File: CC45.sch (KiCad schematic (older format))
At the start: 20 parts, among them J1 AVR-ISP-6, SW1 SW_Push_Dual, U1 ATmega32U4-AU, U2 PRTR5V0U2X, X1 XTAL

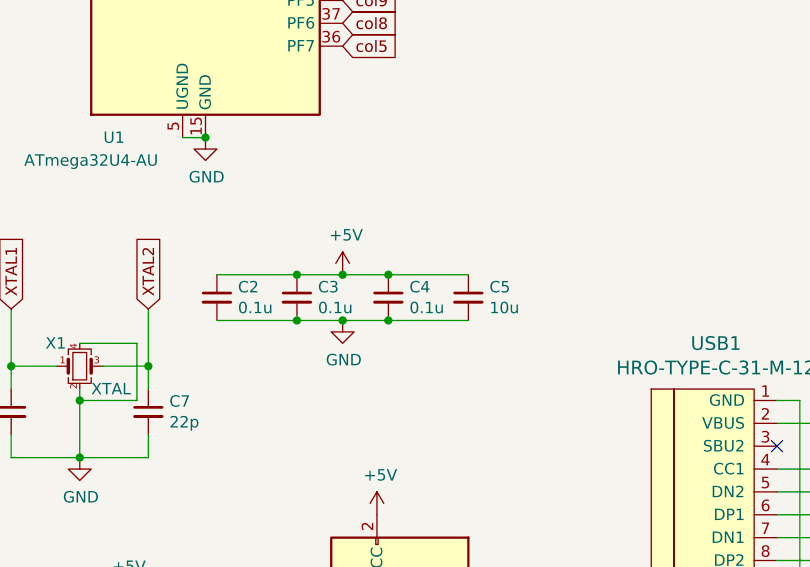
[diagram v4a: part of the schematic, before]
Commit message: Add a decoupling capacitor
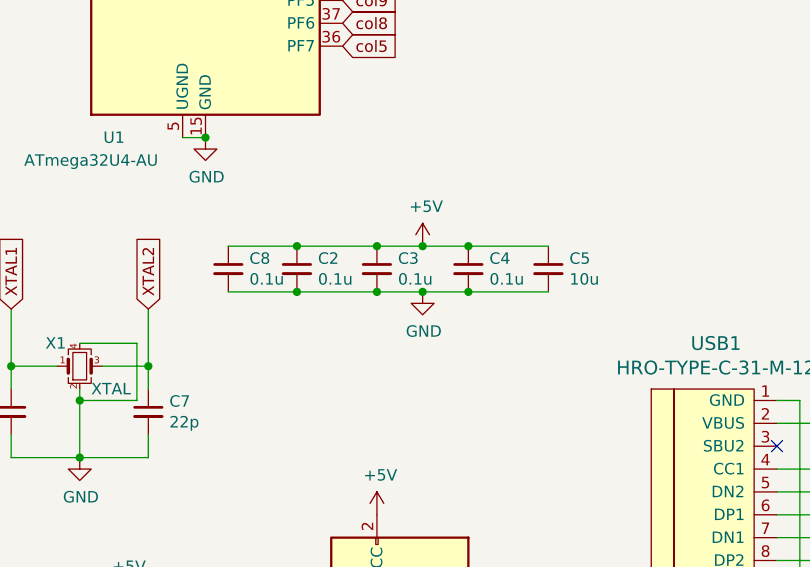
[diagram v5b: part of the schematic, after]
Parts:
- added C8: 0.1u, Capacitor_SMD:C_1206_3216Metric_Pad1.42x1.75mm_HandSolder, symbol Device:C_Small
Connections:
- net +5V: now also C8.1
- net GND: now also C8.2
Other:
- moved on the sheet: C2, C3, C4, C5

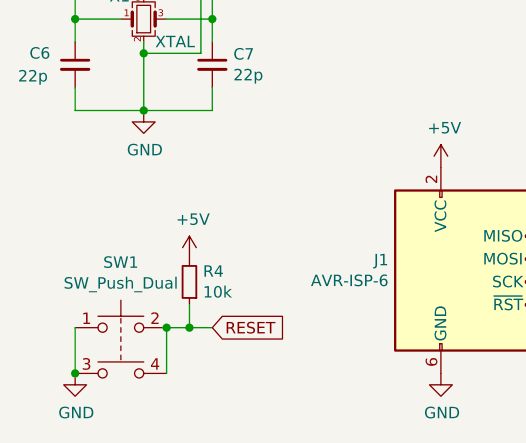
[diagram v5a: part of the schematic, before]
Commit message: Add fill zones
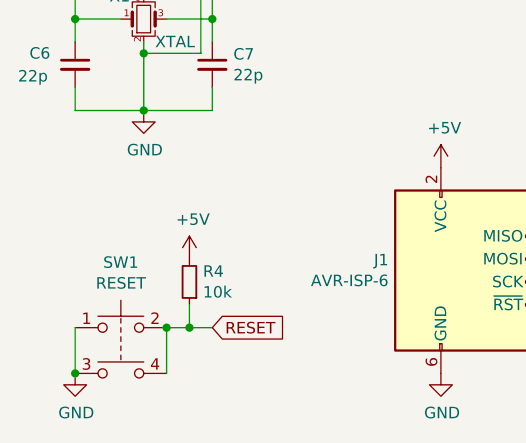
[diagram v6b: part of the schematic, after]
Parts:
- SW1: value SW_Push_Dual -> RESET
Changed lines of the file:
@@
 P 1300 7100
 F 0 "SW1" H 1300 7385 50  0000 C CNN
-F 1 "SW_Push_Dual" H 1300 7294 50  0000 C CNN
+F 1 "RESET" H 1300 7294 50  0000 C CNN
 F 2 "random-keyboard-parts:SKQG-1155865" H 1300 7300 50  0001 C CNN
 F 3 "~" H 1300 7300 50  0001 C CNN

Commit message: moving C4 closer to the mcu and adding JLC parts numbers
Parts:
- C1: LCSC (none) -> C1848
- C2, C3, C4, C8: LCSC (none) -> C24497
- C5: LCSC (none) -> C13585
- C6, C7: LCSC (none) -> C313096
- F1: LCSC (none) -> C151162
- R1, R4: LCSC (none) -> C17902
- R2, R3: LCSC (none) -> C17958
- R5, R6: LCSC (none) -> C26033
- SW1: LCSC (none) -> C318884
- U1: LCSC (none) -> C44854
- U2: LCSC (none) -> C78442
- X1: LCSC (none) -> C13738
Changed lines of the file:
@@
 F 2 "Capacitor_SMD:C_1206_3216Metric_Pad1.42x1.75mm_HandSolder" H 1100 5950 50  0001 C CNN
 F 3 "~" H 1100 5950 50  0001 C CNN
+F 4 "C313096" H 1100 5950 50  0001 C CNN "LCSC"
 	1    1100 5950
 	1    0    0    -1
@@
 F 2 "random-keyboard-parts:SKQG-1155865" H 1300 7300 50  0001 C CNN
 F 3 "~" H 1300 7300 50  0001 C CNN
+F 4 "C318884" H 1300 7100 50  0001 C CNN "LCSC"
 	1    1300 7100
 	1    0    0    -1
@@
 F 2 "Resistor_SMD:R_1206_3216Metric_Pad1.42x1.75mm_HandSolder" H 1600 6900 50  0001 C CNN
 F 3 "~" H 1600 6900 50  0001 C CNN
+F 4 "C17902" H 1600 6900 50  0001 C CNN "LCSC"
 	1    1600 6900
 	-1   0    0    1
@@
 F 2 "Fuse:Fuse_1206_3216Metric_Pad1.42x1.75mm_HandSolder" H 5200 5800 50  0001 L CNN
 F 3 "~" H 5150 6000 50  0001 C CNN
+F 4 "C151162" H 5150 6000 50  0001 C CNN "LCSC"
 	1    5150 6000
 	0    1    1    0
@@
 F 2 "Resistor_SMD:R_1206_3216Metric_Pad1.42x1.75mm_HandSolder" H 4800 6900 50  0001 C CNN
 F 3 "~" H 4800 6900 50  0001 C CNN
+F 4 "C26033" H 4800 6900 50  0001 C CNN "LCSC"
 	1    4800 6900
 	-1   0    0    1
@@
 F 2 "Resistor_SMD:R_1206_3216Metric_Pad1.42x1.75mm_HandSolder" H 5150 6900 50  0001 C CNN
 F 3 "~" H 5150 6900 50  0001 C CNN
+F 4 "C26033" H 5150 6900 50  0001 C CNN "LCSC"
 	1    5150 6900
 	-1   0    0    1
@@
 F 2 "Resistor_SMD:R_1206_3216Metric_Pad1.42x1.75mm_HandSolder" H 6400 6600 50  0001 C CNN
 F 3 "~" H 6400 6600 50  0001 C CNN
+F 4 "C17958" H 6400 6600 50  0001 C CNN "LCSC"
 	1    6400 6600
 	0    1    1    0
@@
 F 2 "Resistor_SMD:R_1206_3216Metric_Pad1.42x1.75mm_HandSolder" H 6400 6500 50  0001 C CNN
 F 3 "~" H 6400 6500 50  0001 C CNN
+F 4 "C17958" H 6400 6500 50  0001 C CNN "LCSC"
 	1    6400 6500
 	0    1    1    0
@@
 F 2 "random-keyboard-parts:SOT143B" H 5800 6900 60  0001 C CNN
 F 3 "" H 5800 6900 60  0001 C CNN
+F 4 "C78442" H 5800 6900 50  0001 C CNN "LCSC"
 	1    5800 6900
 	-1   0    0    1
@@
 F 2 "Capacitor_SMD:C_1206_3216Metric_Pad1.42x1.75mm_HandSolder" H 1700 5950 50  0001 C CNN
 F 3 "~" H 1700 5950 50  0001 C CNN
+F 4 "C313096" H 1700 5950 50  0001 C CNN "LCSC"
 	1    1700 5950
 	1    0    0    -1
@@
 F 2 "Crystal:Crystal_SMD_3225-4Pin_3.2x2.5mm_HandSoldering" H 1400 5750 50  0001 C CNN
 F 3 "~" H 1400 5750 50  0001 C CNN
+F 4 "C13738" H 1400 5750 50  0001 C CNN "LCSC"
 	1    1400 5750
 	1    0    0    -1
@@
 F 2 "Capacitor_SMD:C_1206_3216Metric_Pad1.42x1.75mm_HandSolder" H 2050 5325 50  0001 C CNN
 F 3 "~" H 2050 5325 50  0001 C CNN
+F 4 "C24497" H 2050 5325 50  0001 C CNN "LCSC"
 	1    2050 5325
 	1    0    0    -1
@@
 F 2 "Capacitor_SMD:C_1206_3216Metric_Pad1.42x1.75mm_HandSolder" H 3450 5325 50  0001 C CNN
 F 3 "~" H 3450 5325 50  0001 C CNN
+F 4 "C13585" H 3450 5325 50  0001 C CNN "LCSC"
 	1    3450 5325
 	1    0    0    -1
@@
 F 2 "Capacitor_SMD:C_1206_3216Metric_Pad1.42x1.75mm_HandSolder" H 3100 5325 50  0001 C CNN
 F 3 "~" H 3100 5325 50  0001 C CNN
+F 4 "C24497" H 3100 5325 50  0001 C CNN "LCSC"
 	1    3100 5325
 	1    0    0    -1
@@
 F 2 "Capacitor_SMD:C_1206_3216Metric_Pad1.42x1.75mm_HandSolder" H 2350 5325 50  0001 C CNN
 F 3 "~" H 2350 5325 50  0001 C CNN
+F 4 "C24497" H 2350 5325 50  0001 C CNN "LCSC"
 	1    2350 5325
 	1    0    0    -1
@@
 F 2 "Capacitor_SMD:C_1206_3216Metric_Pad1.42x1.75mm_HandSolder" H 2700 5325 50  0001 C CNN
 F 3 "~" H 2700 5325 50  0001 C CNN
+F 4 "C24497" H 2700 5325 50  0001 C CNN "LCSC"
 	1    2700 5325
 	1    0    0    -1
@@
 F 2 "Package_QFP:TQFP-44_10x10mm_P0.8mm" H 1950 2950 50  0001 C CIN
 F 3 "http://ww1.microchip.com/downloads/en/DeviceDoc/Atmel-7766-8-bit-AVR-ATmega16U4-32U4_Datasheet.pdf" H 1950 2950 50  0001 C CNN
+F 4 "C44854" H 1950 2950 50  0001 C CNN "LCSC"
 	1    1950 2950
 	1    0    0    -1
@@
 F 2 "Resistor_SMD:R_1206_3216Metric_Pad1.42x1.75mm_HandSolder" H 2900 3550 50  0001 C CNN
 F 3 "~" H 2900 3550 50  0001 C CNN
+F 4 "C17902" H 2900 3550 50  0001 C CNN "LCSC"
 	1    2900 3550
 	0    1    1    0
@@
 F 2 "Capacitor_SMD:C_1206_3216Metric_Pad1.42x1.75mm_HandSolder" H 1200 2950 50  0001 C CNN
 F 3 "~" H 1200 2950 50  0001 C CNN
+F 4 "C1848" H 1200 2950 50  0001 C CNN "LCSC"
 	1    1200 2950
 	1    0    0    -1

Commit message: v2 update
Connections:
- net col0: now also U1.32 (PC7); no longer U1.27 (PD7)
- net col1: now also U1.40 (PF1); no longer U1.29 (PB5)
- net col10: now also U1.28 (PB4); no longer U1.39 (PF4)
- net col11: now also U1.29 (PB5); no longer U1.40 (PF1)
- net col12: now also U1.30 (PB6); no longer U1.41 (PF0)
- net col2: now also U1.39 (PF4); no longer U1.30 (PB6)
- net col3: now also U1.38 (PF5); no longer U1.31 (PC6)
- net col4: now also U1.37 (PF6); no longer U1.32 (PC7)
- net col6: now also U1.18 (PD0); no longer U1.12 (PB7)
- net col7: now also U1.19 (PD1); no longer U1.1 (PE6)
- net col8: now also U1.26 (PD6); no longer U1.37 (PF6)
- net col9: now also U1.27 (PD7); no longer U1.38 (PF5)
- net row0: now also U1.41 (PF0); no longer U1.25 (PD4)
- net row1: now also U1.1 (PE6); no longer U1.26 (PD6)
- net row2: now also U1.25 (PD4); no longer U1.28 (PB4)
- net row3: now also U1.31 (PC6); no longer U1.22 (PD5)
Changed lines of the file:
@@
 Text GLabel 2550 1750 2    50   Input ~ 0
 MISO
-Text GLabel 2550 2150 2    50   Input ~ 0
+Text GLabel 2550 2650 2    50   Input ~ 0
 col6
+Text GLabel 2550 3050 2    50   Input ~ 0
+row2
+Text GLabel 2550 2050 2    50   Input ~ 0
+col12
+Text GLabel 2550 1950 2    50   Input ~ 0
+col11
 Text GLabel 2550 1850 2    50   Input ~ 0
-row2
-Text GLabel 2550 3850 2    50   Input ~ 0
-col12
-Text GLabel 2550 3950 2    50   Input ~ 0
-col11
-Text GLabel 2550 4050 2    50   Input ~ 0
 col10
-Text GLabel 2550 4150 2    50   Input ~ 0
+Text GLabel 2550 3350 2    50   Input ~ 0
 col9
-Text GLabel 2550 4250 2    50   Input ~ 0
+Text GLabel 2550 3250 2    50   Input ~ 0
 col8
-Text GLabel 2550 3650 2    50   Input ~ 0
+Text GLabel 2550 2750 2    50   Input ~ 0
 col7
 Text GLabel 2550 4350 2    50   Input ~ 0
 col5
+Text GLabel 2550 4250 2    50   Input ~ 0
+col4
+Text GLabel 2550 4150 2    50   Input ~ 0
+col3
+Text GLabel 2550 4050 2    50   Input ~ 0
+col2
+Text GLabel 2550 3950 2    50   Input ~ 0
+col1
 Text GLabel 2550 2450 2    50   Input ~ 0
-col4
+col0
+Text GLabel 2550 3850 2    50   Input ~ 0
+row0
+Text GLabel 2550 3650 2    50   Input ~ 0
+row1
 Text GLabel 2550 2350 2    50   Input ~ 0
-col3
-Text GLabel 2550 2050 2    50   Input ~ 0
-col2
-Text GLabel 2550 1950 2    50   Input ~ 0
-col1
-Text GLabel 2550 3350 2    50   Input ~ 0
-col0
-Text GLabel 2550 3050 2    50   Input ~ 0
-row0
-Text GLabel 2550 3250 2    50   Input ~ 0
-row1
-Text GLabel 2550 3150 2    50   Input ~ 0
 row3
-NoConn ~ 2550 2650
-NoConn ~ 2550 2750
+NoConn ~ 2550 2150
+NoConn ~ 2550 3150
 NoConn ~ 2550 2850
 NoConn ~ 2550 2950
